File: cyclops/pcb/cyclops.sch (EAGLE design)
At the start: 156 parts, among them Q1 BC817, Q2 IRF510, Q3 BC817, Q4 BC817, U1 MCP4921, U10 TLV2374, U11 THS4281, U12 MAX4564, U13 ZXTD, U14 ZXTD, U3 MAX4564, U4 LT1931, U5 LT1764A, U6 337L, U67 ZLDO1117, U69 LT1716, U7 TLV3701, U8 ADR03, U9 OP1177

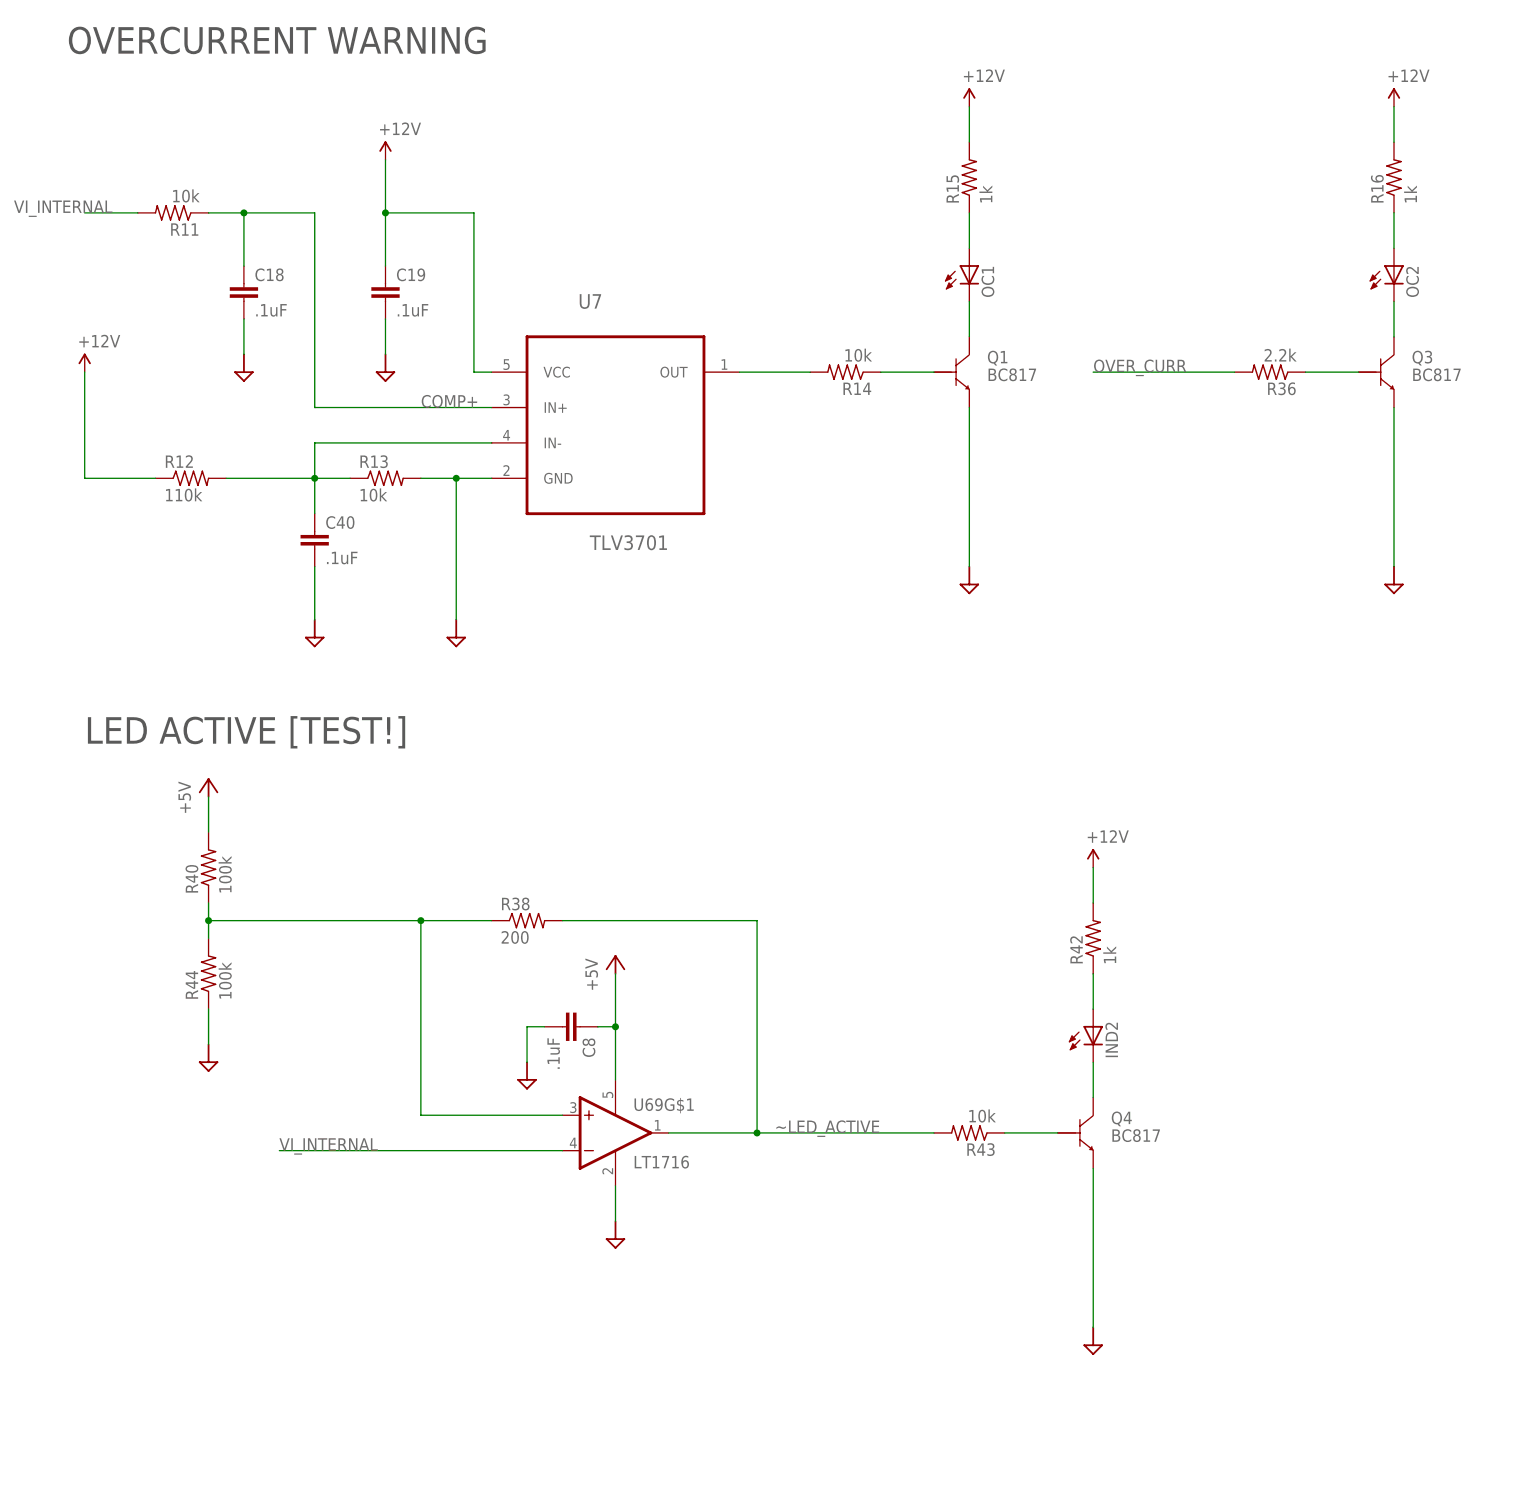
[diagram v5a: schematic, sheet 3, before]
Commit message: Lots of circuit improvments
- Cleaned up/flattened spice folder
- Created a nice high-side current sense circuit in spice that I will
  need to prototype before integrated with cyclops drivetrain
- Physically tested and spice modeled LED active "TTL" signal that will
  can be switched to the VREF output
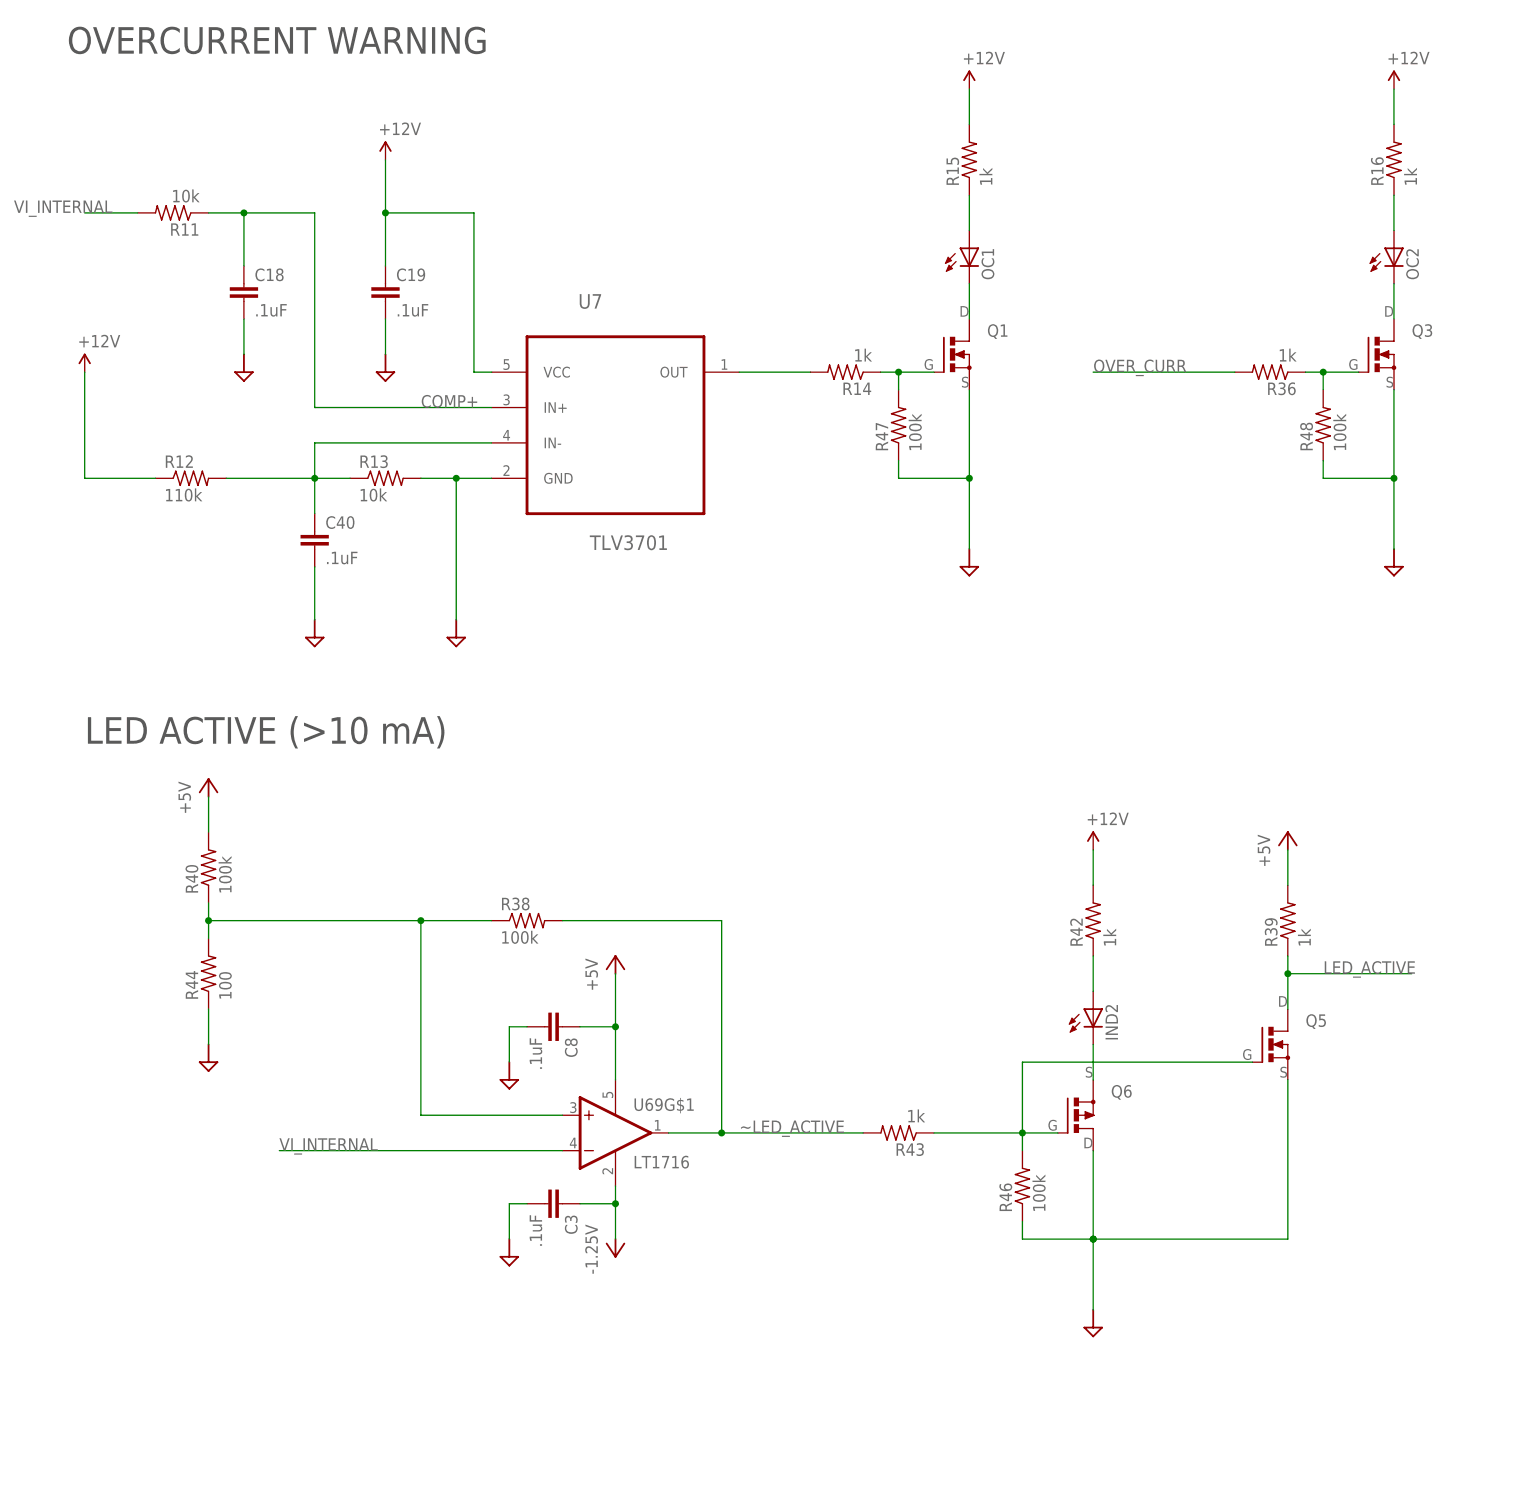
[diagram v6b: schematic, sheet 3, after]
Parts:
- removed Q4: BC817, cyclops:BC817-16SMD
- added C3: .1uF, cyclops:C_0603
- added J_ADDR0, J_ADDR1, J_ADDR2, J_ADDR3: 0, cyclops:R_0603
- added Q5: (no value), jonnew:N-MOSFET_SOT23-GSD
- added Q6: (no value), jonnew:P-MOSFET_SOT23-GSD
- added R39: 1k, cyclops:R_0603
- added R46, R47, R48: 100k, cyclops:R_0603
- Q1, Q3: value BC817 -> (none); device cyclops:BC817-16SMD -> jonnew:N-MOSFET_SOT23-GSD
- R14, R43: value 10k -> 1k
- R36: value 2.2k -> 1k
- R38: value 200 -> 100k
- R44: value 100k -> 100
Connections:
- new net LED_ACTIVE: Q5.D, R39.1, VREF<>TTL.3
- new net N$40: J_ADDR3.2, UC.33/T
- new net N$41: J_ADDR2.2, UC.32/T/PWM
- new net N$44: J_ADDR1.2, UC.31/A20
- new net N$45: J_ADDR0.2, UC.30/A19/SDA1
- net +5V: now also R39.2
- net -1.25V: now also C3.1, U69G$2.V-
- net GND: now also C3.2, J_ADDR0.1, J_ADDR1.1, J_ADDR2.1, J_ADDR3.1, Q1.S, Q3.S, Q5.S, Q6.D, R46.1, R47.1, R48.1; no longer Q1.E, Q3.E, Q4.E, U69G$2.V-
- net N$28: now also Q1.G, R47.2; no longer Q1.B
- net N$39: now also Q3.G, R48.2; no longer Q3.B
- net N$47: now also Q6.S; no longer Q4.C
- net N$49: now also Q5.G, Q6.G, R46.2; no longer Q4.B
- net N$9: now also Q1.D; no longer Q1.C
- net OC: now also Q3.D; no longer Q3.C
- net ~LED_ACTIVE: no longer VREF<>TTL.3
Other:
- note added: "LED ACTIVE (>10 mA)"
- note removed: "LED ACTIVE [TEST!]"
- moved on the sheet: C8, IND2, OC1, OC2, R15, R16, R21, R42, R43

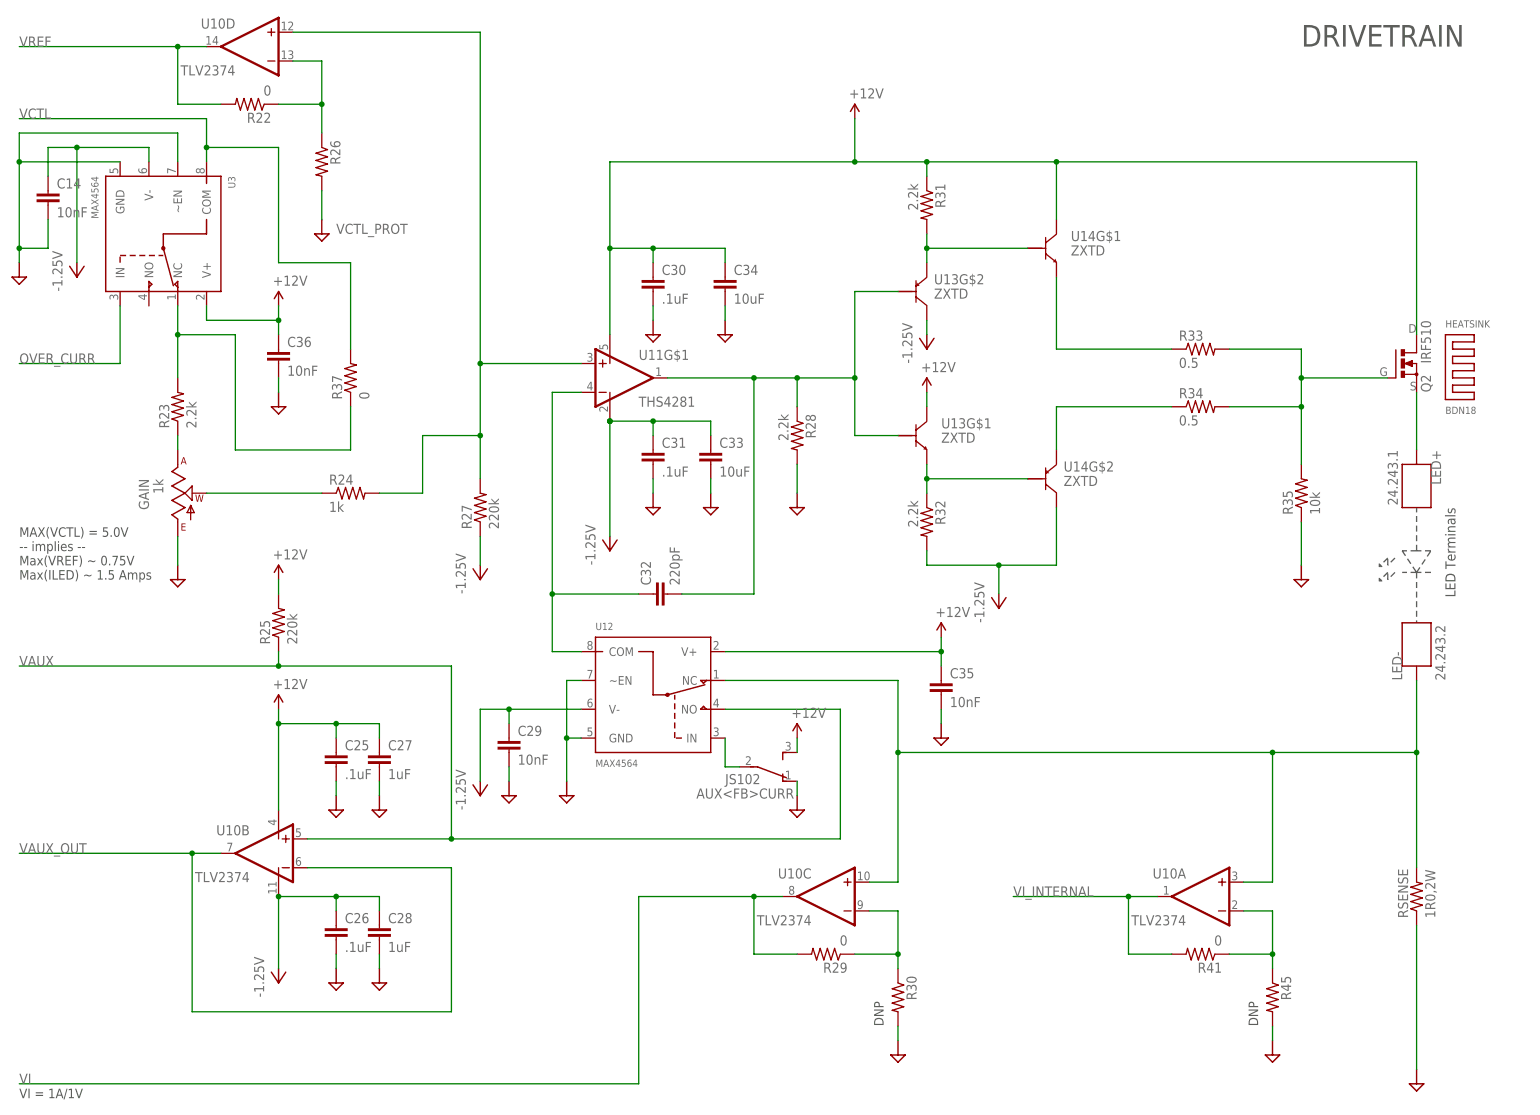
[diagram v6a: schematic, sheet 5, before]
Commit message: Lots of minor circuit mods
- Replace OC SPDT with a SPST with better bandwidth and larger voltage
  rail capabilities since id does not need the other terminal
- Spice modeling of input circuitry
- Etc
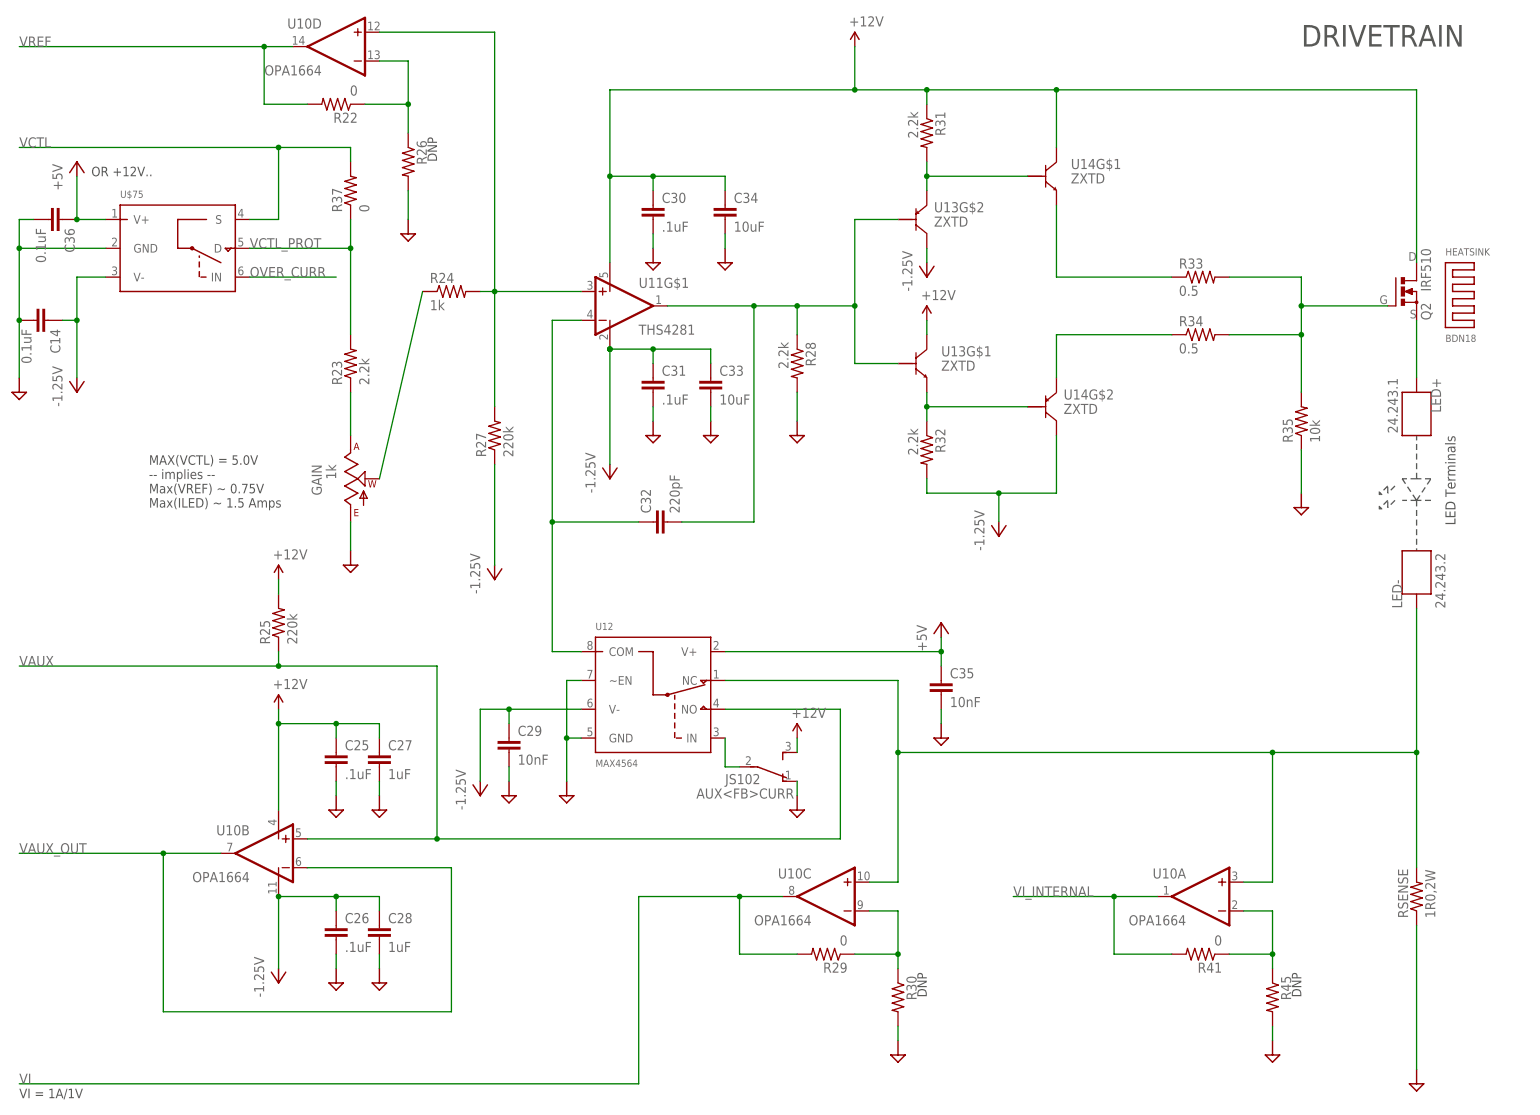
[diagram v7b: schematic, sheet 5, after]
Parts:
- removed Q6: (no value), jonnew:P-MOSFET_SOT23-GSD
- removed R39: 1k, cyclops:R_0603
- removed U3: MAX4564, cyclops:MAX4564
- removed U69: LT1716, jonnew:COMPARITOR_LT1716
- removed U7: TLV3701, ti-extended:TLV3701CDBVT
- added U$75: (no value), jonnew:SPST_IC_SOT23-6
- added U74: TLV3701, jonnew:COMPARITOR_ADCMP600
- added U75: LT1711, jonnew:LT1711
- C14, C36: value 10nF -> 0.1uF
- U10: value TLV2374 -> OPA1664
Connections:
- removed net ~LED_ACTIVE: R38.2, R43.2, U69G$1.OUT
- new net N$50: R38.2, U75G$1.Q
- new net V-: R13.2, U74G$2.V-
- net +12V: now also U74G$2.V+; no longer C35.1, C36.1, U12.V+, U3.V+, U7.VCC
- net +5V: now also C35.1, C36.1, U$75.V+, U12.V+, U75G$2.V+; no longer R39.2, R40.2, U69G$2.V+
- net -1.25V: now also U$75.V-, U75G$2.V-; no longer U3.V-, U69G$2.V-
- net COMP+: now also U74G$1.+IN; no longer U7.IN+
- net GND: now also U$75.GND, U75G$1.GND, U75G$1.LATCH; no longer Q6.D, R13.2, U3.GND, U3.~EN, U7.GND
- net LED_ACTIVE: now also R43.2, U75G$1.~Q; no longer Q5.D, R39.1
- net N$27: now also U74G$1.OUT; no longer U7.OUT
- net N$42: now also U75G$1.+IN; no longer U69G$1.+IN
- net N$47: now also Q5.D; no longer Q6.S
- net N$49: no longer Q6.G
- net N$5: now also U74G$1.-IN; no longer U7.IN-
- net OVER_CURR: no longer U3.IN
- net REF5.0: now also R40.2
- net VCTL: now also U$75.S; no longer U3.COM
- net VCTL_PROT: now also U$75.D; no longer U3.NC
- net VI_INTERNAL: now also U75G$1.-IN; no longer U69G$1.-IN
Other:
- note added: "OR +12V.."
- note added: "OVERCURRENT"
- note added: "TODO: 1. ~~Replace arduino headers with teensy headers (male and female since teensy comes without them)~~ 2. ~~Are the LED arrays mounted at correct distance from board edge?~~ 3.~~ Is teensy at correct distance from board edge?~~ 4. Is there adequare clearance b/w rear panel mount components 5. Rearrange panels to fit changes in front and back 6. +5V regulator layout 7. ~~Test LED ON circuit. Y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"
- note removed: "OVERCURRENT WARNING"
- note removed: "TODO: 1. ~~Replace arduino headers with teensy headers (male and female since teensy comes without them)~~ 2. ~~Are the LED arrays mounted at correct distance from board edge?~~ 3.~~ Is teensy at correct distance from board edge?~~ 4. Is there adequare clearance b/w rear panel mount components 5. Rearrange panels to fit changes in front and back 6. +5V regulator layout 7. Test LED ON circuit. You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"
- moved on the sheet: C14, C3, C30, C31, C32, C33, C34, C36, C40, C8, GAIN, HEATSINK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
